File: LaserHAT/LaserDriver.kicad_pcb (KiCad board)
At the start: 2 copper layers, 65 x 56.5 mm, 5 parts, among them J1 RaspberryPi_2x20_HAT

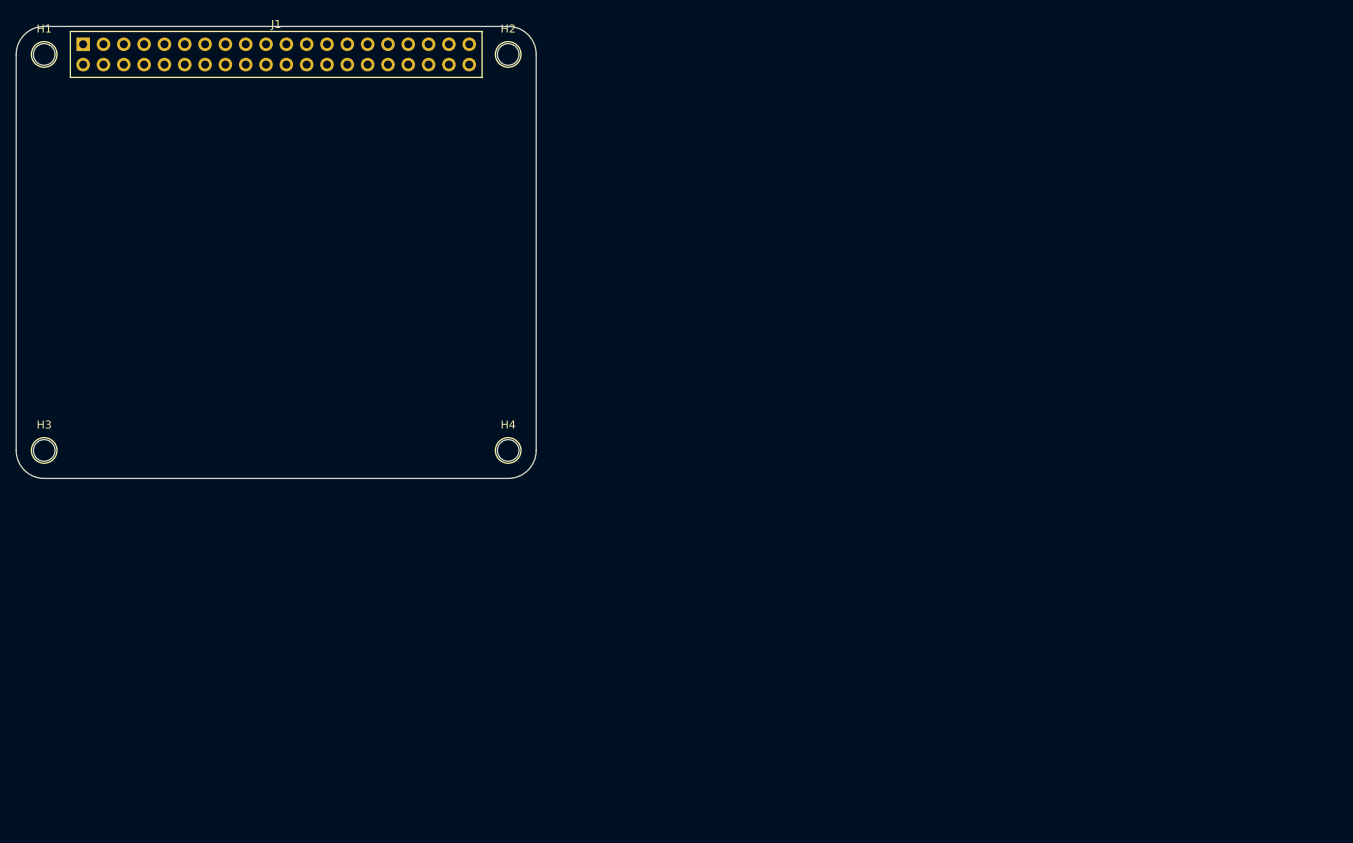
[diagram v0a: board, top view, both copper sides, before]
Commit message: Rebase schematic and PCB from PiHatTemplate
Schematic (LaserDriver.kicad_sch): template taken as base verbatim,
preserving all GPIO connector symbols, pin labels, decoupling caps,
ID EEPROM notes, and solder jumpers exactly as drawn. Paper changed
A4→A3; title block updated. Three sub-sheet boxes (Laser Driver,
MSPM0, USB-C UART) appended at x=230 to avoid overlap with the
template's GPIO content.

PCB (LaserDriver.kicad_pcb): replaced with PiHatTemplate PCB, which
uses the correct PinSocket_2x20 on B.Cu (female, mates with Pi header)
and includes proper board-outline notches, stackup, and mounting holes.
Updated sheetfile reference to LaserDriver.kicad_sch; J1 UUID link
(00000000-0000-0000-0000-000059ad464a) is consistent with schematic.

Added merge_template.py script that performs the merge reproducibly.

Co-Authored-By: Claude Sonnet 4.6 <noreply@anthropic.com>
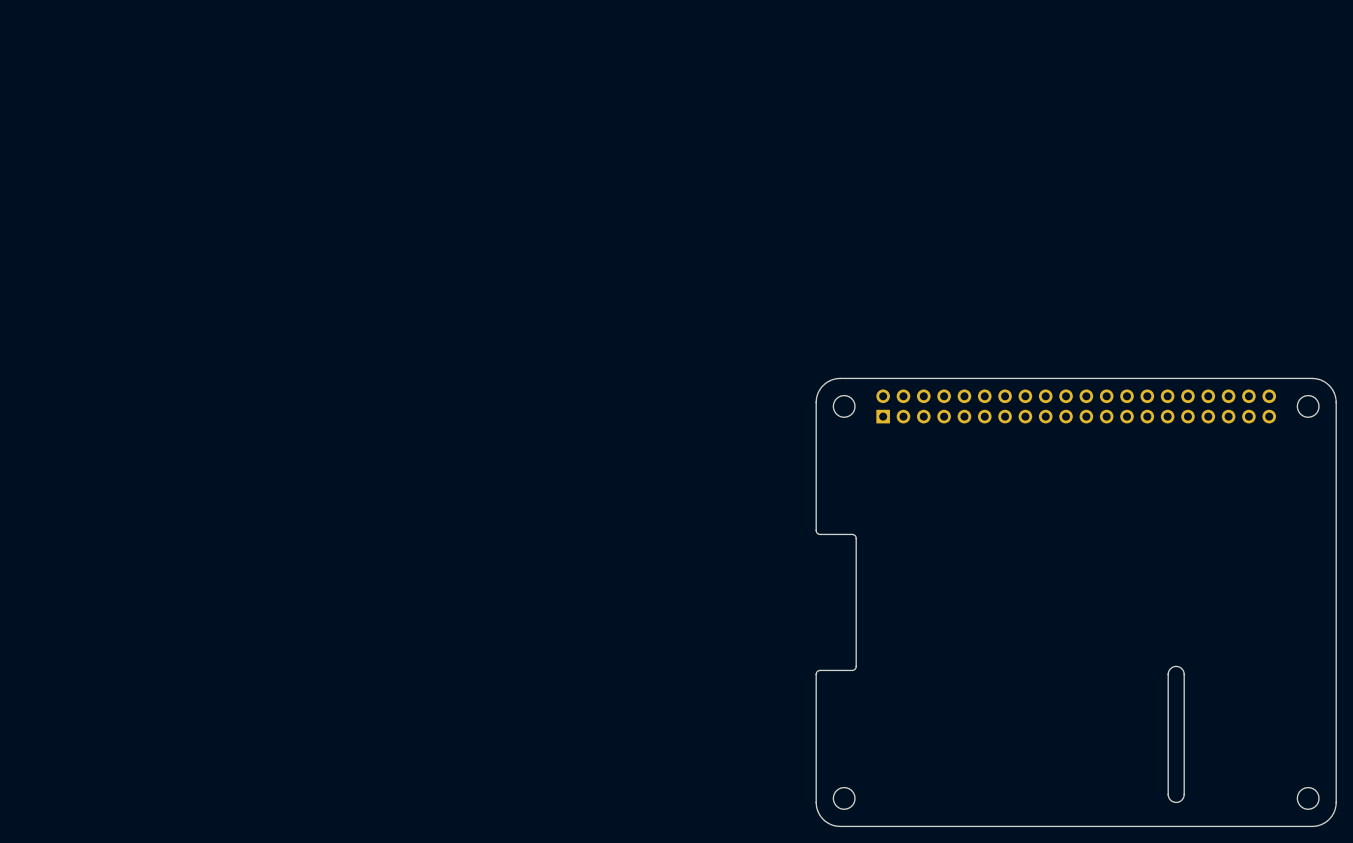
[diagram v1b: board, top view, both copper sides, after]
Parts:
- removed H1, H2, H3, H4: MountingHole_2.7mm_M2.5, MountingHole:MountingHole_2.7mm_M2.5
- added MH1: MountingHole_2.7mm_M2.5, MountingHole:MountingHole_2.7mm_M2.5, F.Cu at (103.5, 47.5)
- added MH2: MountingHole_2.7mm_M2.5, MountingHole:MountingHole_2.7mm_M2.5, F.Cu at (161.5, 47.5)
- added MH3: MountingHole_2.7mm_M2.5, MountingHole:MountingHole_2.7mm_M2.5, F.Cu at (103.5, 96.5)
- added MH4: MountingHole_2.7mm_M2.5, MountingHole:MountingHole_2.7mm_M2.5, F.Cu at (161.5, 96.5)
- J1: value RaspberryPi_2x20_HAT -> GPIO; footprint Connector_PinHeader_2.54mm:PinHeader_2x20_P2.54mm_Vertical -> Connector_PinSocket_2.54mm:PinSocket_2x20_P2.54mm_Vertical; moved to B.Cu
- moved J1 110.3 mm to (108.4, 48.8), turned to -90 degrees
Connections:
- J1 pad 1: (no net) -> +3V3
- J1 pad 10: (no net) -> /GPIO15/RXD0
- J1 pad 11: (no net) -> /GPIO17
- J1 pad 12: (no net) -> /GPIO18/PCM.CLK
- J1 pad 13: (no net) -> /GPIO27
- J1 pad 14: (no net) -> GND
- J1 pad 15: (no net) -> /GPIO22
- J1 pad 16: (no net) -> /GPIO23
- J1 pad 17: (no net) -> +3V3
- J1 pad 18: (no net) -> /GPIO24
- J1 pad 19: (no net) -> /GPIO10/SPI0.MOSI
- J1 pad 2: (no net) -> +5V
- J1 pad 20: (no net) -> GND
- J1 pad 21: (no net) -> /GPIO9/SPI0.MISO
- J1 pad 22: (no net) -> /GPIO25
- J1 pad 23: (no net) -> /GPIO11/SPI0.SCLK
- J1 pad 24: (no net) -> /GPIO8/SPI0.CE0
- J1 pad 25: (no net) -> GND
- J1 pad 26: (no net) -> /GPIO7/SPI0.CE1
- J1 pad 27: (no net) -> /ID_SDA
- J1 pad 28: (no net) -> /ID_SCL
- J1 pad 29: (no net) -> /GPIO5
- J1 pad 3: (no net) -> /GPIO2/SDA1
- J1 pad 30: (no net) -> GND
- J1 pad 31: (no net) -> /GPIO6
- J1 pad 32: (no net) -> /GPIO12/PWM0
- J1 pad 33: (no net) -> /GPIO13/PWM1
- J1 pad 34: (no net) -> GND
- J1 pad 35: (no net) -> /GPIO19/PCM.FS
- J1 pad 36: (no net) -> /GPIO16
- J1 pad 37: (no net) -> /GPIO26
- J1 pad 38: (no net) -> /GPIO20/PCM.DIN
- J1 pad 39: (no net) -> GND
- J1 pad 4: (no net) -> +5V
- J1 pad 40: (no net) -> /GPIO21/PCM.DOUT
- J1 pad 5: (no net) -> /GPIO3/SCL1
- J1 pad 6: (no net) -> GND
- J1 pad 7: (no net) -> /GPIO4/GPCLK0
- J1 pad 8: (no net) -> /GPIO14/TXD0
- J1 pad 9: (no net) -> GND
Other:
- board size 65 x 56.5 mm -> 65 x 56 mm
- board text added: "CAMERA (OPTIONAL)"
- board text added: "DISPLAY (OPTIONAL)"
- board text added: "Extend PCB edge 0.5mm if using SMT header"
- board text added: "PoE"
- board text added: "RJ45"
- board text added: "USB"
